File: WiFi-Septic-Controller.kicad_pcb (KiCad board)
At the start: 2 copper layers, 80 x 90 mm, 104 parts, among them J1 Screw_Terminal_01x02, J2 Screw_Terminal_01x02, J3 Screw_Terminal_01x03, J4 Screw_Terminal_01x06, J5 USB_B_Micro, J6 GWT-C1627A-RGB, J7 Cortex Debug, J8 Screw_Terminal_01x03, Q1 2N7002, Q2 2N7002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

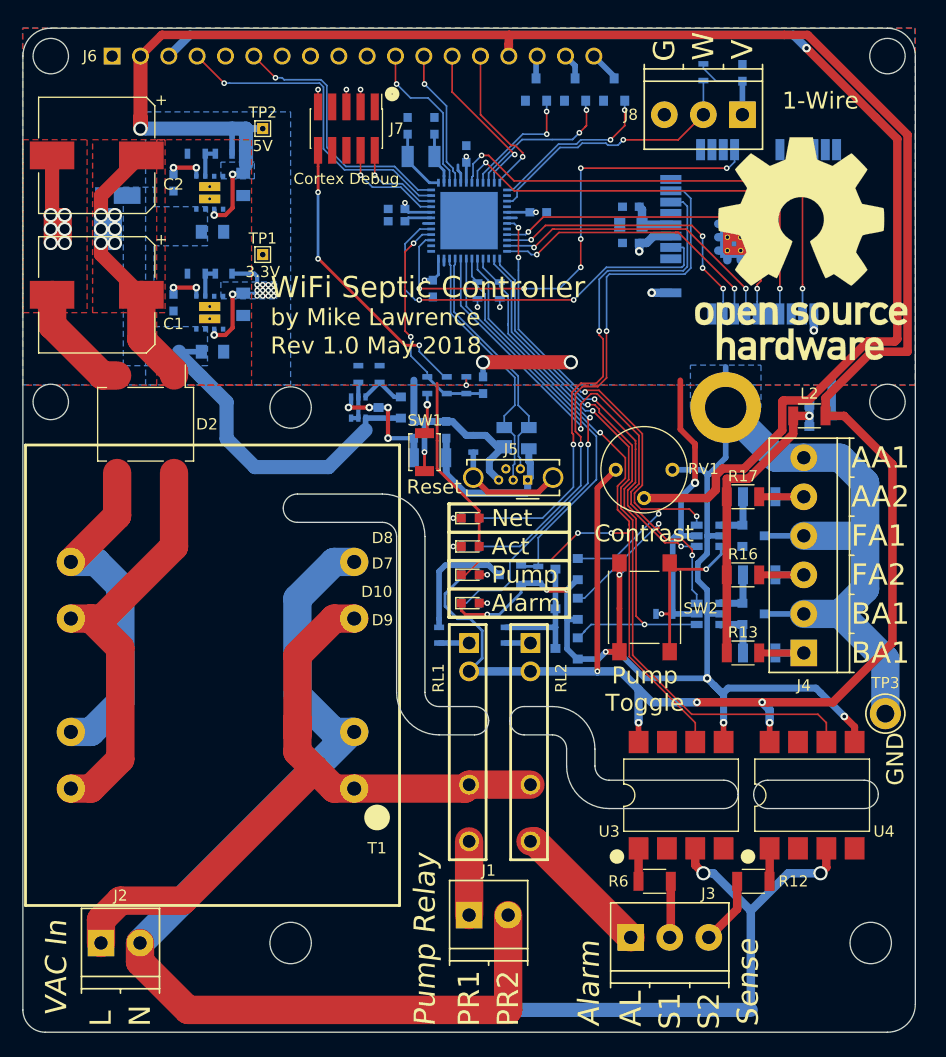
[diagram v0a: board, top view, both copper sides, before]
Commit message: Update to KiCad 5.1 libraries.
Also updated custom libraries.
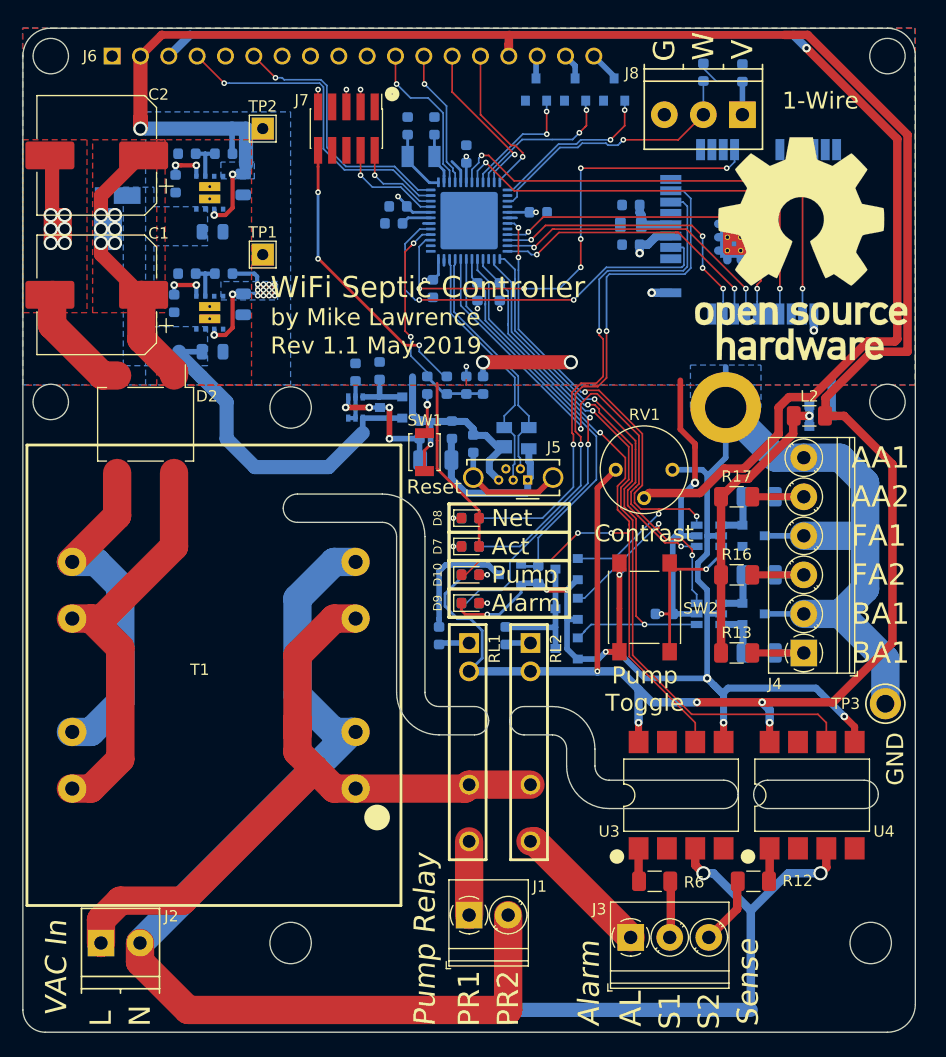
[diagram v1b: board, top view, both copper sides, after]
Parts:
- C1, C2: footprint Capacitors_SMD:CP_Elec_10x10.5 -> Capacitor_SMD:CP_Elec_10x10.5
- C10, C17, C3, C5, C8: footprint Capacitors_SMD:C_0805 -> Capacitor_SMD:C_0805_2012Metric
- C11, C12, C13, C14, C15, C16, C18, C19, C20, C21, C22, C4, C6, C7, C9: footprint Capacitors_SMD:C_0603 -> Capacitor_SMD:C_0603_1608Metric
- D1: footprint Diodes_SMD:D_PowerDI-123 -> Diode_SMD:D_PowerDI-123
- D10, D7, D8, D9: footprint LEDs:LED_0603 -> LED_SMD:LED_0603_1608Metric
- D2: footprint Diodes_SMD:Diode_Bridge_DFS -> Diode_SMD:Diode_Bridge_Vishay_DFS
- D3, D4, D5, Q1, Q2, Q3, Q5, Q6, Q7, Q8, Q9: footprint TO_SOT_Packages_SMD:SOT-23 -> Package_TO_SOT_SMD:SOT-23
- D6: footprint TO_SOT_Packages_SMD:SOT-143 -> Package_TO_SOT_SMD:SOT-143
- J1: footprint TerminalBlock_Phoenix:TerminalBlock_Phoenix_PT-3.5mm_2pol -> TerminalBlock_Phoenix:TerminalBlock_Phoenix_PT-1,5-2-3.5-H_1x02_P3.50mm_Horizontal
- J3: footprint TerminalBlock_Phoenix:TerminalBlock_Phoenix_PT-3.5mm_3pol -> TerminalBlock_Phoenix:TerminalBlock_Phoenix_PT-1,5-3-3.5-H_1x03_P3.50mm_Horizontal
- J4: footprint TerminalBlock_Phoenix:TerminalBlock_Phoenix_PT-3.5mm_6pol -> TerminalBlock_Phoenix:TerminalBlock_Phoenix_PT-1,5-6-3.5-H_1x06_P3.50mm_Horizontal
- J5: footprint Connectors_USB:USB_Micro-B_Wuerth-614105150721_Vertical_CircularHoles -> Connector_USB:USB_Micro-B_Wuerth_614105150721_Vertical_CircularHoles
- J6: footprint adafruit-ml:GWT-C1627A-RGB -> Adafruit-ML:GWT-C1627A-RGB
- J7: footprint Pin_Headers:Pin_Header_Straight_2x05_Pitch1.27mm_SMD -> Connector_PinHeader_1.27mm:PinHeader_2x05_P1.27mm_Vertical_SMD
- L1, L2: footprint Inductors_SMD:L_1206 -> Inductor_SMD:L_1206_3216Metric
- L3: footprint Inductors_SMD:L_0603 -> Inductor_SMD:L_0603_1608Metric
- MK1: footprint holes-ml:6-32_PTH_Mounting_Hole -> MountingHole-ML:6-32_PTH_Mounting_Hole
- Q4: footprint TO_SOT_Packages_SMD:SOT-363_SC-70-6 -> Package_TO_SOT_SMD:SOT-363_SC-70-6
- R1, R10, R11, R19, R2, R20, R21, R22, R23, R24, R25, R26, R28, R29, R3, R4, R5, R7, R8, R9: footprint Resistors_SMD:R_0603 -> Resistor_SMD:R_0603_1608Metric
- R12, R6: footprint Resistors_SMD:R_1206 -> Resistor_SMD:R_1206_3216Metric
- R13, R14, R15, R16, R17, R18: value 100k -> 22k; footprint Resistors_SMD:R_1206 -> Resistor_SMD:R_1206_3216Metric
- RL1, RL2: footprint ixys-ml:SIP-4 -> Relay_THT-ML:Relay_IXYS_PowerSIP
- RV1: footprint Potentiometers:Potentiometer_Trimmer_Bourns_3339P_Horizontal -> Potentiometer_THT:Potentiometer_Bourns_3339P_Vertical
- SW1: footprint Buttons_Switches_SMD:SW_SPST_B3U-1000P -> Button_Switch_SMD:SW_SPST_B3U-1000P
- SW2: footprint Buttons_Switches_SMD:SW_SPST_PTS645 -> Button_Switch_SMD:SW_SPST_PTS645
- T1: footprint triad-ml:VPP -> Transformer_THT-ML:Triad_VPP_5.0VA
- TP1, TP2: footprint Connectors_TestPoints:Test_Point_THTPad_1.0x1.0mm_Drill0.5mm -> TestPoint:TestPoint_THTPad_2.0x2.0mm_Drill1.0mm
- TP3: footprint Connectors_TestPoints:Test_Point_Keystone_5010-5014_Multipurpose -> TestPoint:TestPoint_Keystone_5010-5014_Multipurpose
- U1, U2: footprint ti-ml:SIL0008E -> Converter_DCDC-ML:Converter_DCDC_Texas-SIL0008E
- U3, U4: footprint Housings_DIP:SMDIP-8_W9.53mm -> Package_DIP:SMDIP-8_W9.53mm
- U5, U7: footprint TO_SOT_Packages_SMD:SOT-23-6 -> Package_TO_SOT_SMD:SOT-23-6
- U6: footprint atmel-ml:ATWINC1500-MR210XB -> RF_Module-ML:Microchip_ATWINC1500-MR210UB
- U8: footprint Housings_DFN_QFN:QFN-48-1EP_7x7mm_Pitch0.5mm -> Package_DFN_QFN:QFN-48-1EP_7x7mm_P0.5mm_EP5.15x5.15mm
- Y1: footprint abracon-ml:ABS07 -> Crystal-ML:Crystal_SMD_Abracon_ABS07-2Pin_3.2x1.5mm
- moved TP3 0.89 mm to (107.3, 90.6)
- moved R2 0.80 mm to (44.7, 52.0)
- moved R8 0.80 mm to (44.7, 41.2)
- moved R13 0.57 mm to (94.0, 86.0)
- moved R16 0.57 mm to (94.0, 79.0)
- moved R17 0.57 mm to (94.0, 72.0)
- moved L1 0.55 mm to (67.0, 68.7)
- moved C7 0.51 mm to (65.6, 66.0)
- moved C6 0.51 mm to (68.5, 66.0)
- moved C16 0.32 mm to (63.2, 47.5)
- moved R9 0.30 mm to (59.8, 60.8)
- moved R10 0.29 mm to (62.0, 60.7)
- moved C12 0.26 mm to (63.6, 46.0)
- moved Q4 0.25 mm to (59.8, 64.0)
- moved C9 0.21 mm to (43.7, 43.9)
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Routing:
- net Net-(Q3-Pad1): track 4.26 -> 5.17 mm
- net Net-(C7-Pad2): track 11.5 -> 12.4 mm
- net Net-(J6-Pad3): track 118.8 -> 117.9 mm
- net Net-(R7-Pad2): track 2.92 -> 3.78 mm
- net Net-(R1-Pad2): track 2.92 -> 3.78 mm
- net VCC: track 89.2 -> 89.9 mm
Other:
- board text added: "Rev 1.1 May 2019"
- board text removed: "Rev 1.0 May 2018"
